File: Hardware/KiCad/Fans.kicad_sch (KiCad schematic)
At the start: 16 parts, among them Q1 IRLML0030, Q2 IRLML0030

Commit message: finished LCSC
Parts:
- FANS1, TACH_A1, TACH_B1: now left out of the parts list
- PD_TACHA1, PD_TACHB1: LCSC (none) -> C25804
- PWM_A1, PWM_B1: footprint TestPoint:TestPoint_Keystone_5000-5004_Miniature -> Connector_PinHeader_2.54mm:PinHeader_1x01_P2.54mm_Vertical; now left out of the parts list
- Q1, Q2: LCSC (none) -> C67272
- R_G1, R_G2: LCSC (none) -> C22356636
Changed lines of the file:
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@@
 			)
 		)
-		(property "LCSC" ""
+		(property "LCSC" "C25804"
 			(at 87.63 83.82 90)
 			(effects
@@
 			)
 		)
-		(property "LCSC" ""
+		(property "LCSC" "C22356636"
 			(at 107.95 107.95 90)
 			(effects
@@
 			)
 		)
-		(property "LCSC" ""
+		(property "LCSC" "C25804"
 			(at 87.63 64.77 90)
 			(effects
@@
 		(unit 1)
 		(exclude_from_sim no)
-		(in_bom yes)
+		(in_bom no)
 		(on_board yes)
 		(dnp no)
@@
 			)
 		)
-		(property "Footprint" "TestPoint:TestPoint_Keystone_5000-5004_Miniature"
+		(property "Footprint" "Connector_PinHeader_2.54mm:PinHeader_1x01_P2.54mm_Vertical"
 			(at 106.68 107.95 0)
 			(effects
@@
 			)
 		)
+		(property "LCSC" "C67272"
+			(at 124.46 107.95 0)
+			(effects
+				(font
+					(size 1.27 1.27)
+				)
+				(hide yes)
+			)
+		)
 		(pin "3"
 		)
@@
 		(unit 1)
 		(exclude_from_sim no)
-		(in_bom yes)
+		(in_bom no)
 		(on_board yes)
 		(dnp no)
@@
 		(unit 1)
 		(exclude_from_sim no)
-		(in_bom yes)
+		(in_bom no)
 		(on_board yes)
 		(dnp no)
@@
 			)
 		)
-		(property "LCSC" ""
+		(property "LCSC" "C22356636"
 			(at 168.91 107.95 90)
 			(effects
@@
 		(unit 1)
 		(exclude_from_sim no)
-		(in_bom yes)
+		(in_bom no)
 		(on_board yes)
 		(dnp no)
@@
 			)
 		)
-		(property "Footprint" "TestPoint:TestPoint_Keystone_5000-5004_Miniature"
+		(property "Footprint" "Connector_PinHeader_2.54mm:PinHeader_1x01_P2.54mm_Vertical"
 			(at 170.18 107.95 0)
 			(effects
@@
 		(unit 1)
 		(exclude_from_sim no)
-		(in_bom yes)
+		(in_bom no)
 		(on_board yes)
 		(dnp no)
@@
 			(at 152.4 107.95 0)
 			(effects
+				(font
+					(size 1.27 1.27)
+				)
+				(hide yes)
+			)
+		)
+		(property "LCSC" "C67272"
+			(at 152.4 107.95 0)
+			(effects

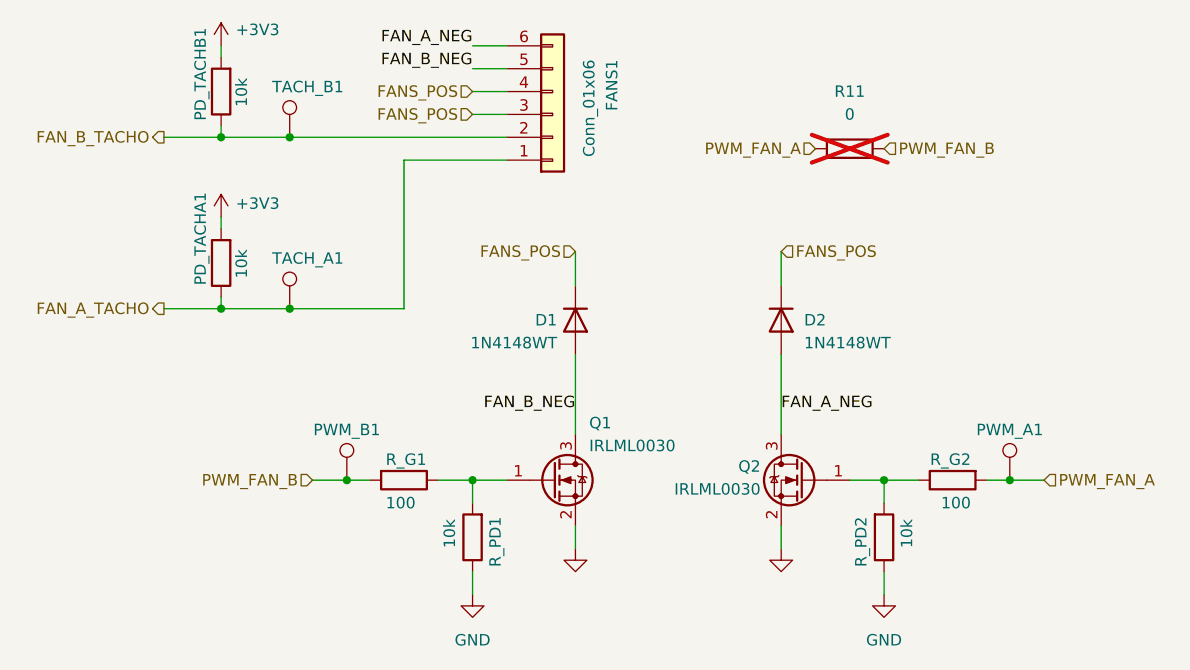
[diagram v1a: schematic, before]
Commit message: fixed references and changed the labels
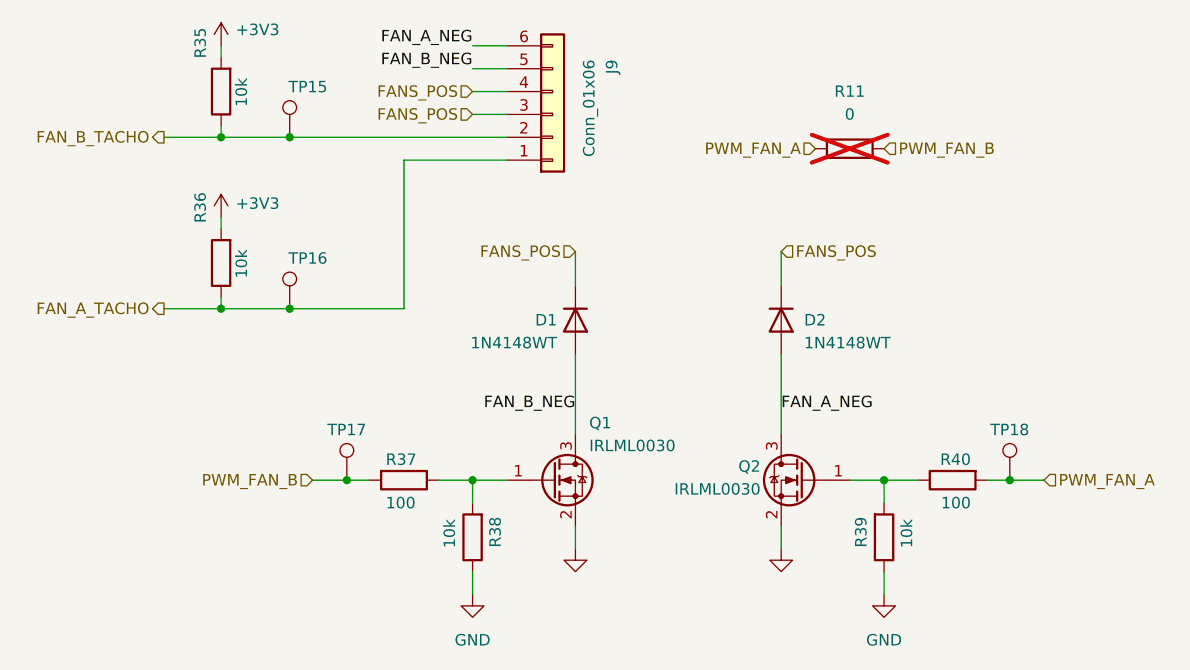
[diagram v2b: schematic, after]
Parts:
- renumbered FANS1 to J9, PD_TACHB1 to R35, PD_TACHA1 to R36, R_G1 to R37, R_PD1 to R38, R_PD2 to R39, R_G2 to R40, TACH_B1 to TP15, TACH_A1 to TP16, PWM_B1 to TP17, PWM_A1 to TP18
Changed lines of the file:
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@@
 		(on_board yes)
 		(dnp no)
-		(property "Reference" "PD_TACHA1"
+		(property "Reference" "R36"
 			(at 85.344 75.946 90)
 			(effects
@@
 			(project "PS-MotorControllerInterfacePCB"
 				(path "/a2e13c19-ff3a-4e43-a7f5-200fd5b2b978/26b9ca43-4422-48e7-9562-1bb32842f27e"
-					(reference "PD_TACHA1")
+					(reference "R36")
 					(unit 1)
 				)
@@
 		(on_board yes)
 		(dnp no)
-		(property "Reference" "R_G1"
+		(property "Reference" "R37"
 			(at 105.918 105.664 90)
 			(effects
@@
 			(project "PS-MotorControllerInterfacePCB"
 				(path "/a2e13c19-ff3a-4e43-a7f5-200fd5b2b978/26b9ca43-4422-48e7-9562-1bb32842f27e"
-					(reference "R_G1")
+					(reference "R37")
 					(unit 1)
 				)
@@
 		(on_board yes)
 		(dnp no)
-		(property "Reference" "PD_TACHB1"
+		(property "Reference" "R35"
 			(at 85.344 57.658 90)
 			(effects
@@
 			(project "PS-MotorControllerInterfacePCB"
 				(path "/a2e13c19-ff3a-4e43-a7f5-200fd5b2b978/26b9ca43-4422-48e7-9562-1bb32842f27e"
-					(reference "PD_TACHB1")
+					(reference "R35")
 					(unit 1)
 				)
@@
 		(on_board yes)
 		(dnp no)
-		(property "Reference" "PWM_B1"
+		(property "Reference" "TP17"
 			(at 101.6 102.362 0)
 			(effects
@@
 			(project ""
 				(path "/a2e13c19-ff3a-4e43-a7f5-200fd5b2b978/26b9ca43-4422-48e7-9562-1bb32842f27e"
-					(reference "PWM_B1")
+					(reference "TP17")
 					(unit 1)
 				)
@@
 		(on_board yes)
 		(dnp no)
-		(property "Reference" "TACH_B1"
+		(property "Reference" "TP15"
 			(at 97.282 64.262 0)
 			(effects
@@
 			(project "PS-MotorControllerInterfacePCB"
 				(path "/a2e13c19-ff3a-4e43-a7f5-200fd5b2b978/26b9ca43-4422-48e7-9562-1bb32842f27e"
-					(reference "TACH_B1")
+					(reference "TP15")
 					(unit 1)
 				)
@@
 		(on_board yes)
 		(dnp no)
-		(property "Reference" "R_PD1"
+		(property "Reference" "R38"
 			(at 118.11 112.014 90)
 			(effects
@@
 			(project "PS-MotorControllerInterfacePCB"
 				(path "/a2e13c19-ff3a-4e43-a7f5-200fd5b2b978/26b9ca43-4422-48e7-9562-1bb32842f27e"
-					(reference "R_PD1")
+					(reference "R38")
 					(unit 1)
 				)
@@
 		(on_board yes)
 		(dnp no)
-		(property "Reference" "FANS1"
+		(property "Reference" "J9"
 			(at 131.064 61.214 90)
 			(effects
@@
 			(project "PS-MotorControllerInterfacePCB"
 				(path "/a2e13c19-ff3a-4e43-a7f5-200fd5b2b978/26b9ca43-4422-48e7-9562-1bb32842f27e"
-					(reference "FANS1")
+					(reference "J9")
 					(unit 1)
 				)
@@
 		(on_board yes)
 		(dnp no)
-		(property "Reference" "R_PD2"
+		(property "Reference" "R39"
 			(at 158.75 112.014 90)
 			(effects
@@
 			(project "PS-MotorControllerInterfacePCB"
 				(path "/a2e13c19-ff3a-4e43-a7f5-200fd5b2b978/26b9ca43-4422-48e7-9562-1bb32842f27e"
-					(reference "R_PD2")
+					(reference "R39")
 					(unit 1)
 				)
@@
 		(on_board yes)
 		(dnp no)
-		(property "Reference" "R_G2"
+		(property "Reference" "R40"
 			(at 170.942 105.664 90)
 			(effects
@@
 			(project "PS-MotorControllerInterfacePCB"
 				(path "/a2e13c19-ff3a-4e43-a7f5-200fd5b2b978/26b9ca43-4422-48e7-9562-1bb32842f27e"
-					(reference "R_G2")
+					(reference "R40")
 					(unit 1)
 				)
@@
 		(on_board yes)
 		(dnp no)
-		(property "Reference" "PWM_A1"
+		(property "Reference" "TP18"
 			(at 175.26 102.362 0)
 			(effects
@@
 			(project "PS-MotorControllerInterfacePCB"
 				(path "/a2e13c19-ff3a-4e43-a7f5-200fd5b2b978/26b9ca43-4422-48e7-9562-1bb32842f27e"
-					(reference "PWM_A1")
+					(reference "TP18")
 					(unit 1)
 				)
@@
 		(on_board yes)
 		(dnp no)
-		(property "Reference" "TACH_A1"
+		(property "Reference" "TP16"
 			(at 97.282 83.312 0)
 			(effects
@@
 			(project "PS-MotorControllerInterfacePCB"
 				(path "/a2e13c19-ff3a-4e43-a7f5-200fd5b2b978/26b9ca43-4422-48e7-9562-1bb32842f27e"
-					(reference "TACH_A1")
+					(reference "TP16")
 					(unit 1)
 				)
